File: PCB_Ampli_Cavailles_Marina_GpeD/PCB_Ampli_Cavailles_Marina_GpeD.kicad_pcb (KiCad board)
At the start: 2 copper layers, 52 parts, among them J2 Conn_01x02, J3 Conn_01x03, Q1 2N2907, Q10 TIP32, Q11 BD138, Q12 TIP31, Q13 2N2222, Q2 2N2907, Q3 2N2907, Q4 2N2222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

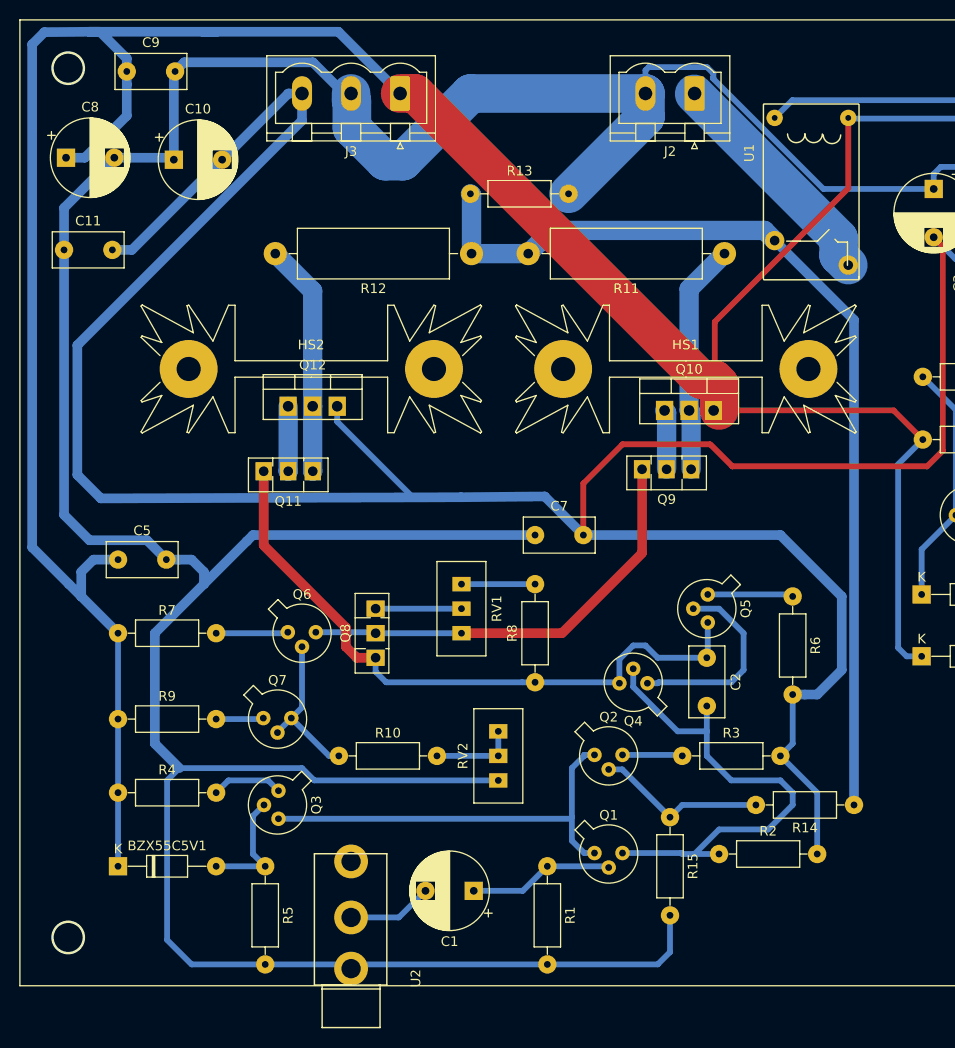
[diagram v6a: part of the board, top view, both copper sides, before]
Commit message: Cambiadas las orientaciones de las alimentaciones y la salida
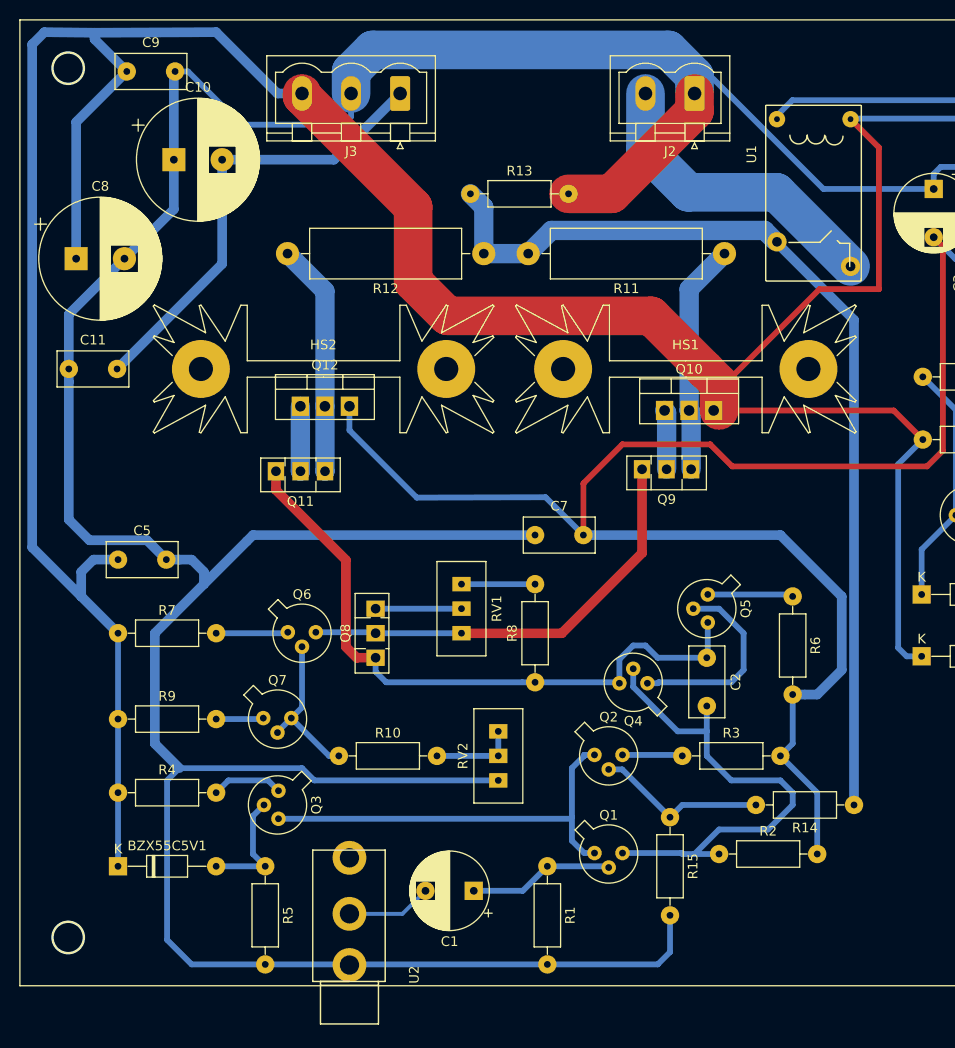
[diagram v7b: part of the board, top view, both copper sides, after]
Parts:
- C1, C3: value CP -> 47u
- C10, C8: value CP -> 470u; footprint CmpAmpliAudio:CP_Radial_D8.0mm_P5.00mm -> CmpAmpliAudioTR:CP_Radial_D12.5mm_P5.00mm
- C11, C5, C7, C9: value C -> 100n
- C4, C6: value CP -> 10u
- moved C11 12.3 mm to (30.5, 61.5)
- moved C8 10.5 mm to (31.2, 50.1)
- moved HS2 1.27 mm to (56.8, 61.5)
- moved Q11 1.27 mm to (57.0, 72.1)
- moved Q12 1.27 mm to (54.4, 65.4)
- moved R12 1.27 mm to (73.4, 49.6)
- moved U2 0.41 mm to (59.5, 125.4)
- moved U1 0.27 mm to (94.3, 10.6)
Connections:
- J2 pad 1: Net-(J2-Pad1) -> GND
- J2 pad 2: GND -> Net-(J2-Pad2)
- J3 pad 1: +12V -> -12V
- J3 pad 3: -12V -> +12V
- U1 pad c2: Net-(J2-Pad1) -> Net-(J2-Pad2)
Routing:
- net -12V: track 287.8 -> 217.5 mm
- net Net-(J2-Pad2): track 0.00 -> 32.0 mm
- net Net-(J2-Pad1): track 24.3 -> 0.00 mm
- net +12V: track 303.0 -> 324.8 mm
- net GND: track 402.5 -> 399.1 mm
- net Net-(R11-Pad2): track 101.1 -> 100.1 mm
- net Net-(C2-Pad1): track 68.8 -> 68.2 mm

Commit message: Cambios menores
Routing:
- net -12V: track 217.5 -> 248.0 mm
- net +12V: track 324.8 -> 316.8 mm
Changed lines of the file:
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@@
     (thickness 1.6)
     (drawings 27)
-    (tracks 272)
+    (tracks 273)
     (zones 0)
     (modules 52)
@@
   )
   (setup
-    (last_trace_width 4)
+    (last_trace_width 0.6)
     (user_trace_width 0.6)
     (user_trace_width 1)
@@
   (segment (start 27.94 26.67) (end 33.12922 26.73096) (width 1) (layer B.Cu) (net 1))
   (segment (start 33.12922 26.73096) (end 45.72 26.67) (width 1) (layer B.Cu) (net 1))
-  (segment (start 54.61 33.282066) (end 66.1162 44.788266) (width 4) (layer F.Cu) (net 1))
   (segment (start 54.61 33.02) (end 54.61 33.282066) (width 4) (layer F.Cu) (net 1))
-  (segment (start 66.1162 52.4891) (end 69.66712 56.04002) (width 4) (layer F.Cu) (net 1))
-  (segment (start 66.1162 44.788266) (end 66.1162 52.4891) (width 4) (layer F.Cu) (net 1))
   (segment (start 97.788661 63.076799) (end 97.788661 65.8368) (width 4) (layer F.Cu) (net 1))
-  (segment (start 69.66712 56.04002) (end 90.751882 56.04002) (width 4) (layer F.Cu) (net 1))
   (segment (start 97.348661 60.585999) (end 96.323261 61.611399) (width 0.6) (layer F.Cu) (net 1))
-  (segment (start 90.751882 56.04002) (end 96.323261 61.611399) (width 4) (layer F.Cu) (net 1))
   (segment (start 96.323261 61.611399) (end 97.788661 63.076799) (width 4) (layer F.Cu) (net 1))
   (segment (start 115.86972 65.8368) (end 97.22866 65.8368) (width 0.6) (layer F.Cu) (net 1))
-  (segment (start 111.4044 35.67966) (end 114.34318 38.61844) (width 0.6) (layer F.Cu) (net 1))
-  (segment (start 114.34318 38.61844) (end 114.34318 53.2765) (width 0.6) (layer F.Cu) (net 1))
   (segment (start 97.22866 64.2368) (end 97.22866 65.8368) (width 0.6) (layer F.Cu) (net 1))
-  (segment (start 108.18896 53.2765) (end 97.22866 64.2368) (width 0.6) (layer F.Cu) (net 1))
-  (segment (start 114.34318 53.2765) (end 108.18896 53.2765) (width 0.6) (layer F.Cu) (net 1))
+  (segment (start 89.009442 54.29758) (end 90.751882 56.04002) (width 4) (layer F.Cu) (net 1))
+  (segment (start 90.751882 56.04002) (end 96.323261 61.611399) (width 4) (layer F.Cu) (net 1))
+  (segment (start 67.57416 54.29758) (end 89.009442 54.29758) (width 4) (layer F.Cu) (net 1))
+  (segment (start 54.61 33.02) (end 54.61 41.33342) (width 4) (layer F.Cu) (net 1))
+  (segment (start 54.61 41.33342) (end 67.57416 54.29758) (width 4) (layer F.Cu) (net 1))
+  (segment (start 111.4044 35.67966) (end 114.13236 38.40762) (width 0.6) (layer F.Cu) (net 1))
+  (segment (start 114.13236 64.09944) (end 115.86972 65.8368) (width 0.6) (layer F.Cu) (net 1))
+  (segment (start 114.13236 38.40762) (end 114.13236 64.09944) (width 0.6) (layer F.Cu) (net 1))
   (segment (start 50.67 106.68) (end 49.53 107.82) (width 0.6) (layer B.Cu) (net 2))
   (segment (start 49.53 107.82) (end 49.53 111.76) (width 0.6) (layer B.Cu) (net 2))
@@
   (segment (start 87.78494 69.34454) (end 83.74 73.38948) (width 0.6) (layer F.Cu) (net 8))
   (segment (start 79.82078 74.82078) (end 83.74 78.74) (width 0.6) (layer B.Cu) (net 8))
-  (segment (start 59.51982 65.39992) (end 59.51982 67.88404) (width 0.6) (layer B.Cu) (net 8))
-  (segment (start 59.51982 67.88404) (end 66.4972 74.86142) (width 0.6) (layer B.Cu) (net 8))
-  (segment (start 66.4972 74.86142) (end 79.82078 74.82078) (width 0.6) (layer B.Cu) (net 8))
   (segment (start 46.3385 50.66538) (end 46.3385 39.87292) (width 1) (layer B.Cu) (net 8))
   (segment (start 35.46476 61.53912) (end 46.3385 50.66538) (width 1) (layer B.Cu) (net 8))
   (segment (start 57.91708 39.87292) (end 46.3385 39.87292) (width 1) (layer B.Cu) (net 8))
   (segment (start 64.77 33.02) (end 57.91708 39.87292) (width 1) (layer B.Cu) (net 8))
+  (segment (start 67.34068 74.82078) (end 79.82078 74.82078) (width 0.6) (layer B.Cu) (net 8))
+  (segment (start 59.51982 66.99992) (end 67.34068 74.82078) (width 0.6) (layer B.Cu) (net 8))
+  (segment (start 59.51982 65.39992) (end 59.51982 66.99992) (width 0.6) (layer B.Cu) (net 8))
+  (segment (start 59.51982 53.05424) (end 46.3385 39.87292) (width 0.6) (layer B.Cu) (net 8))
+  (segment (start 59.51982 65.39992) (end 59.51982 53.05424) (width 0.6) (layer B.Cu) (net 8))
   (segment (start 60.13 123.19) (end 59.69 123.63) (width 0.6) (layer B.Cu) (net 9))
   (segment (start 80.01 123.19) (end 60.13 123.19) (width 0.6) (layer B.Cu) (net 9))
